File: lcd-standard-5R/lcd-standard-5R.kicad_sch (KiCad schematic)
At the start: 4 parts

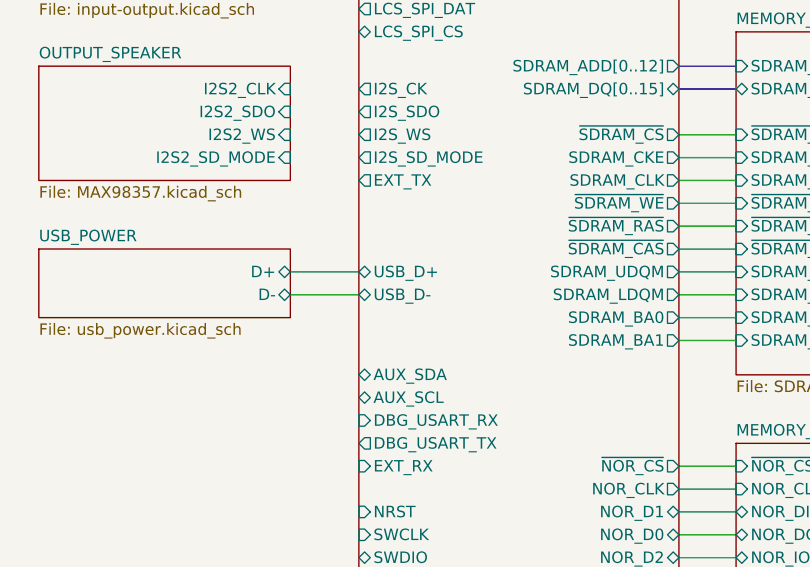
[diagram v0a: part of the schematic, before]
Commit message: Change pinout to the optimum usage
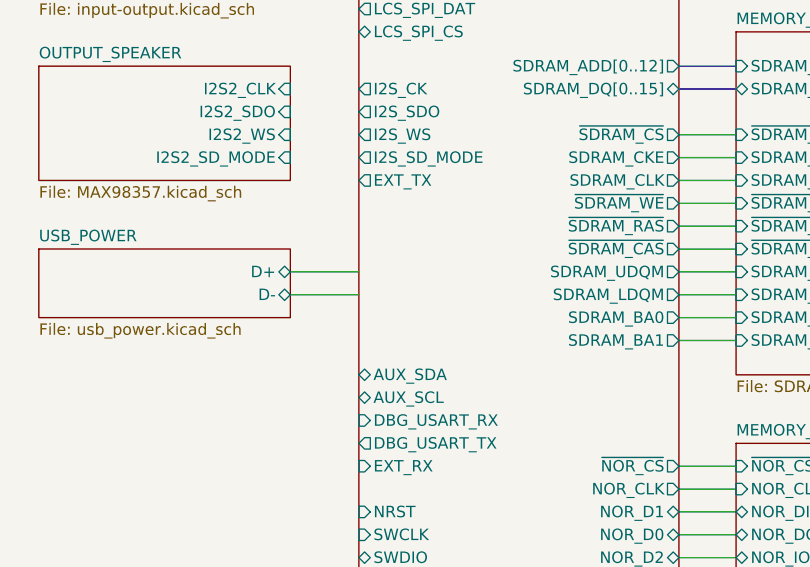
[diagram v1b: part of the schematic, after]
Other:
- sheet MCU ports: added none; removed USB_D+, USB_D-
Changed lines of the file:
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@@
-			)
-		)
-		(pin "USB_D-" bidirectional
-			(at 114.3 121.92 180)
-			(effects
-				(font
-					(size 1.27 1.27)
-				)
-				(justify left)
-			)
-		)
-		(pin "USB_D+" bidirectional
-			(at 114.3 119.38 180)
-			(effects
-				(font
-					(size 1.27 1.27)
-				)
-				(justify left)
 			)
 		)

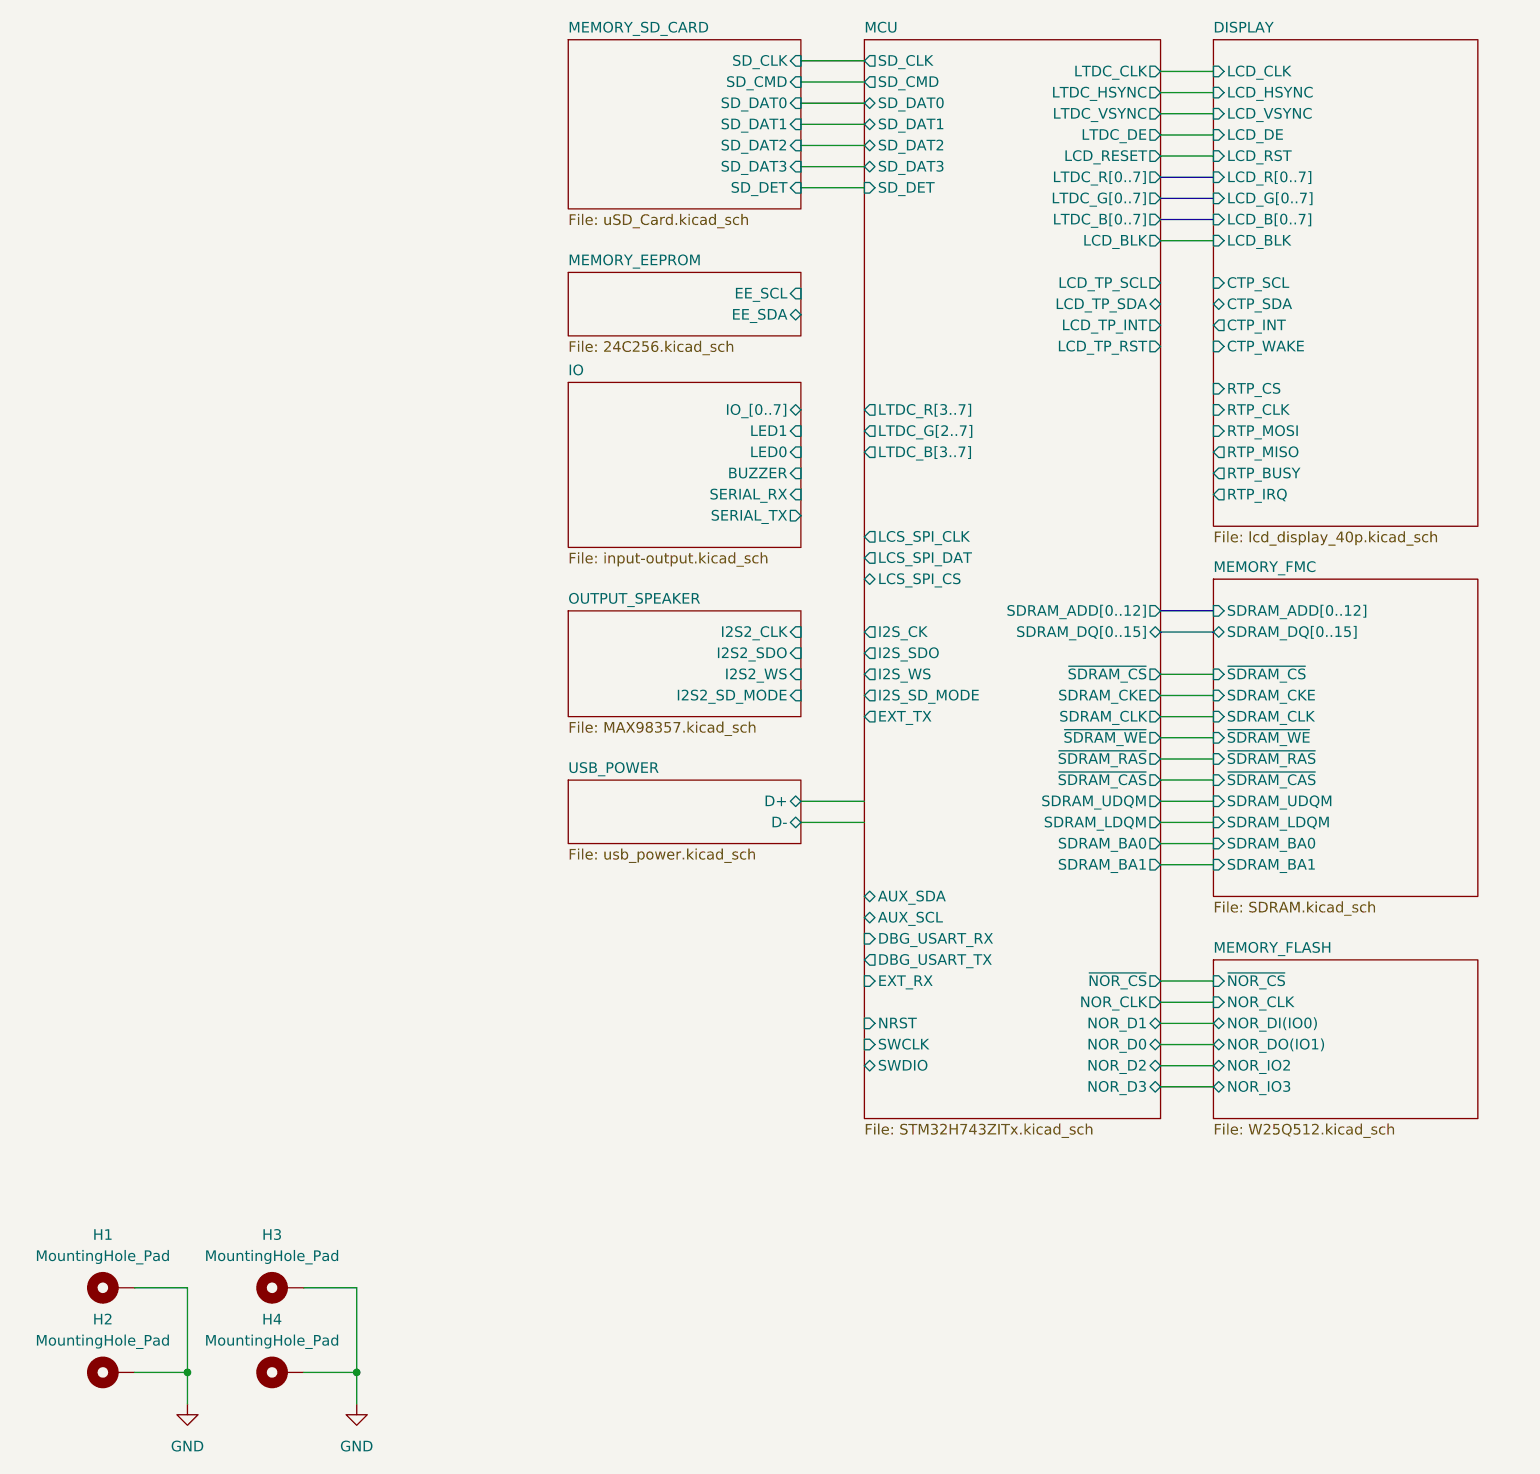
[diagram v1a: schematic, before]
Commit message: Finished SDRAM, LCD (need checkup with CubeIDE), RTP touch controll
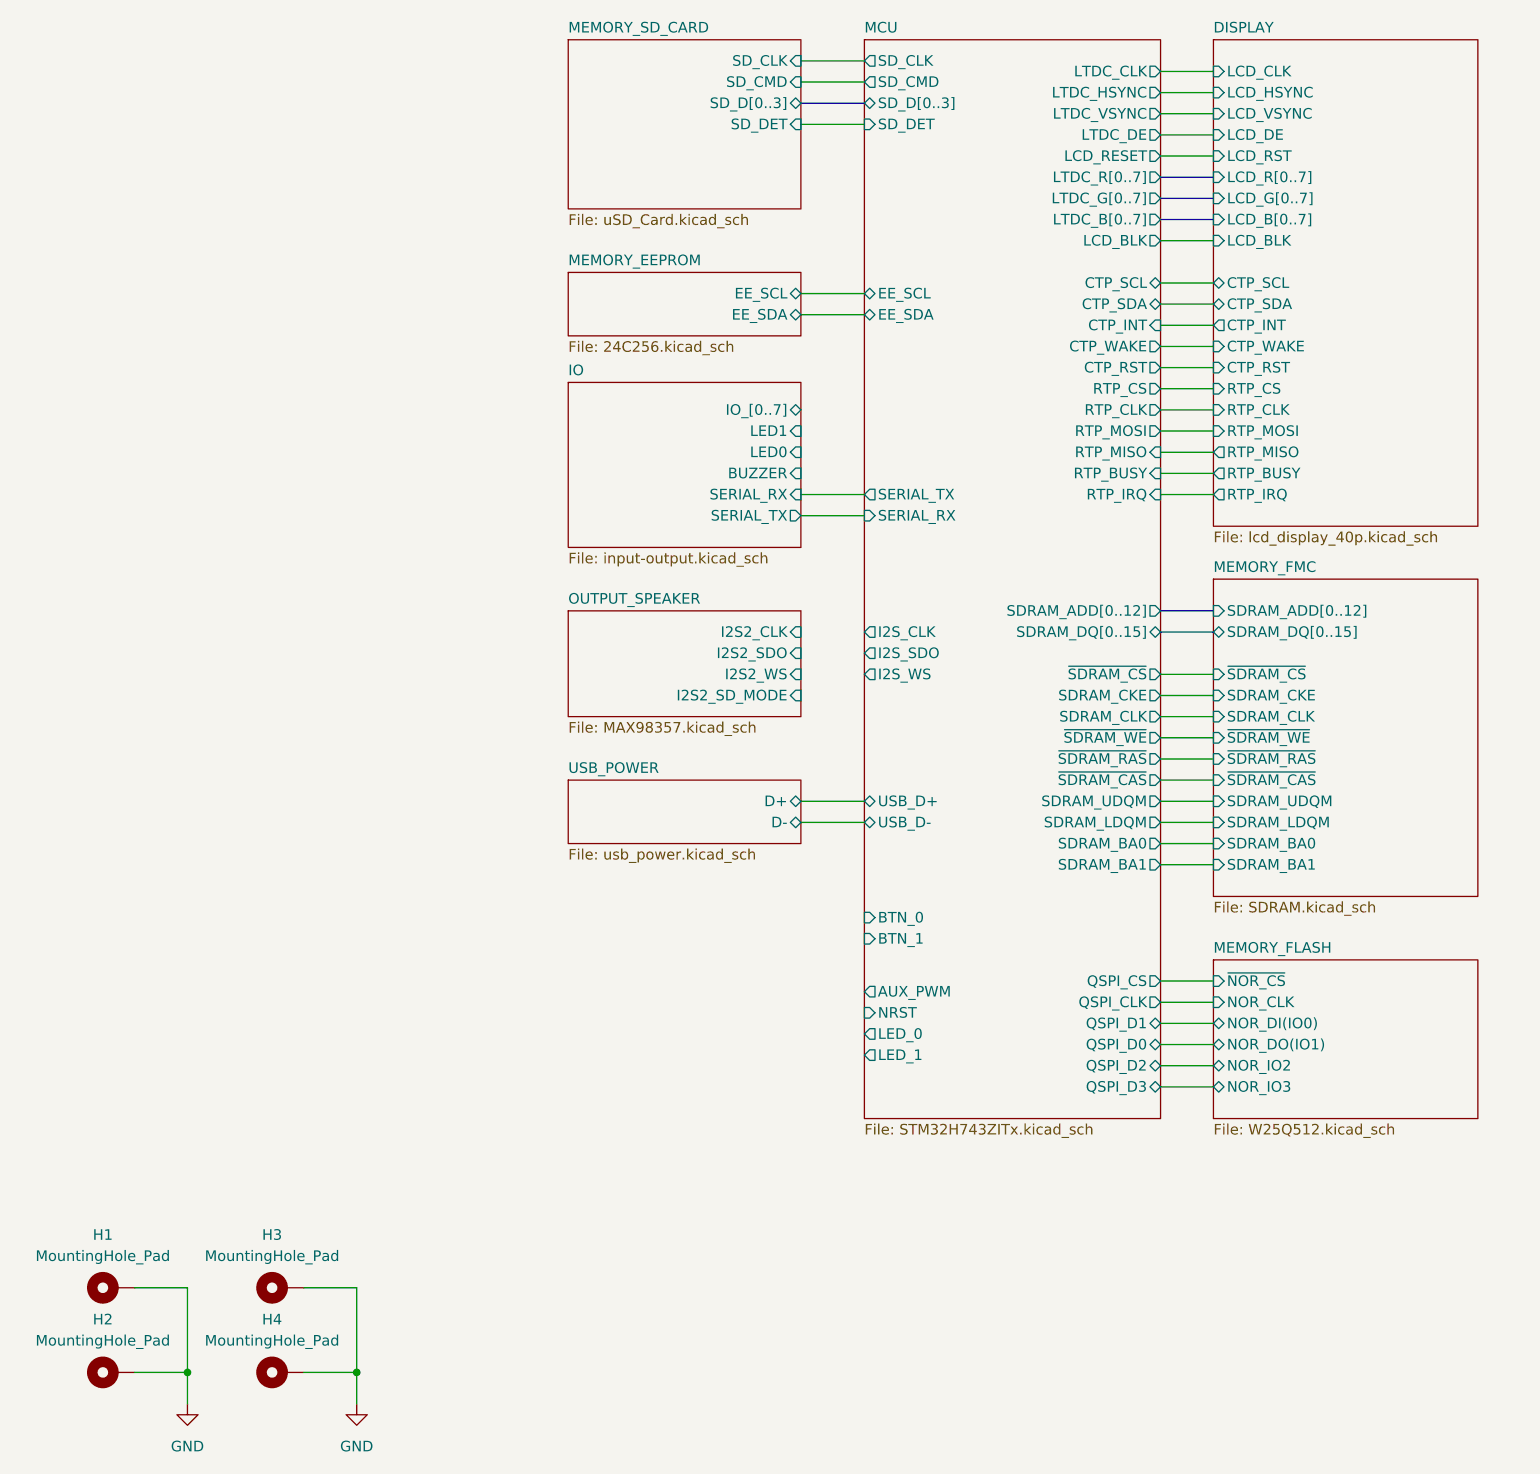
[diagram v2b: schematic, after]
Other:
- sheet DISPLAY ports: added CTP_RST; removed none
- sheet MCU ports: added AUX_PWM, BTN_0, BTN_1, CTP_INT, CTP_RST, CTP_SCL, CTP_SDA, CTP_WAKE, EE_SCL, EE_SDA, I2S_CLK, LED_0, LED_1, QSPI_CLK, QSPI_CS, QSPI_D0, QSPI_D1, QSPI_D2, QSPI_D3, RTP_BUSY, RTP_CLK, RTP_CS, RTP_IRQ, RTP_MISO, RTP_MOSI, SD_D[0..3], SERIAL_RX, SERIAL_TX, USB_D+, USB_D-; removed AUX_SCL, AUX_SDA, DBG_USART_RX, DBG_USART_TX, EXT_RX, EXT_TX, I2S_CK, I2S_SD_MODE, LCD_TP_INT, LCD_TP_RST, LCD_TP_SCL, LCD_TP_SDA, LCS_SPI_CLK, LCS_SPI_CS, LCS_SPI_DAT, LTDC_B[3..7], LTDC_G[2..7], LTDC_R[3..7], NOR_CLK, NOR_D0, NOR_D1, NOR_D2, NOR_D3, SD_DAT0, SD_DAT1, SD_DAT2, SD_DAT3, SWCLK, SWDIO, ~{NOR_CS}
- sheet MEMORY_SD_CARD ports: added SD_D[0..3]; removed SD_DAT0, SD_DAT1, SD_DAT2, SD_DAT3

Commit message: Finsihed, need to touch up a bit
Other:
- sheet IO ports: added BTN_0, BTN_1; removed none
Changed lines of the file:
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@@
+	(wire
+		(pts
+			(xy 106.68 80.01) (xy 114.3 80.01)
+		)
+		(stroke
+			(width 0)
+			(type default)
+		)
+	)
 	(wire
 		(pts
@@
 	(wire
 		(pts
+			(xy 106.68 124.46) (xy 114.3 124.46)
+		)
+		(stroke
+			(width 0)
+			(type default)
+		)
+	)
+	(wire
+		(pts
 			(xy 149.86 57.15) (xy 156.21 57.15)
 		)
@@
 	(wire
 		(pts
+			(xy 106.68 74.93) (xy 114.3 74.93)
+		)
+		(stroke
+			(width 0)
+			(type default)
+		)
+	)
+	(wire
+		(pts
 			(xy 149.86 143.51) (xy 156.21 143.51)
 		)
@@
 	(wire
 		(pts
-			(xy 106.68 85.09) (xy 114.3 85.09)
+			(xy 106.68 93.98) (xy 114.3 93.98)
 		)
 		(stroke
@@
 	(wire
 		(pts
+			(xy 106.68 127) (xy 114.3 127)
+		)
+		(stroke
+			(width 0)
+			(type default)
+		)
+	)
+	(wire
+		(pts
 			(xy 149.86 148.59) (xy 156.21 148.59)
 		)
@@
 	(wire
 		(pts
-			(xy 106.68 119.38) (xy 114.3 119.38)
+			(xy 106.68 142.24) (xy 114.3 142.24)
+		)
+		(stroke
+			(width 0)
+			(type default)
+		)
+	)
+	(wire
+		(pts
+			(xy 106.68 121.92) (xy 114.3 121.92)
 		)
 		(stroke
@@
 	(wire
 		(pts
+			(xy 106.68 77.47) (xy 114.3 77.47)
+		)
+		(stroke
+			(width 0)
+			(type default)
+		)
+	)
+	(wire
+		(pts
 			(xy 149.86 74.93) (xy 156.21 74.93)
 		)
@@
 	(wire
 		(pts
+			(xy 106.68 86.36) (xy 114.3 86.36)
+		)
+		(stroke
+			(width 0)
+			(type default)
+		)
+	)
+	(wire
+		(pts
 			(xy 149.86 121.92) (xy 156.21 121.92)
 		)
@@
 	(wire
 		(pts
-			(xy 106.68 121.92) (xy 114.3 121.92)
+			(xy 106.68 144.78) (xy 114.3 144.78)
 		)
 		(stroke
@@
 	(wire
 		(pts
+			(xy 106.68 82.55) (xy 114.3 82.55)
+		)
+		(stroke
+			(width 0)
+			(type default)
+		)
+	)
+	(wire
+		(pts
 			(xy 149.86 59.69) (xy 156.21 59.69)
 		)
@@
 	(wire
 		(pts
-			(xy 106.68 82.55) (xy 114.3 82.55)
+			(xy 106.68 91.44) (xy 114.3 91.44)
 		)
 		(stroke
@@
 	)
 	(sheet
-		(at 78.74 116.84)
+		(at 78.74 139.7)
 		(size 27.94 7.62)
 		(fields_autoplaced yes)
@@
 		)
 		(property "Sheetname" "USB_POWER"
-			(at 78.74 116.1284 0)
+			(at 78.74 138.9884 0)
 			(effects
 				(font
@@
 		)
 		(property "Sheetfile" "usb_power.kicad_sch"
-			(at 78.74 125.0446 0)
+			(at 78.74 147.9046 0)
 			(effects
 				(font
@@
 		)
 		(pin "D+" bidirectional
-			(at 106.68 119.38 0)
+			(at 106.68 142.24 0)
 			(effects
 				(font
@@
 		)
 		(pin "D-" bidirectional
-			(at 106.68 121.92 0)
+			(at 106.68 144.78 0)
 			(effects
 				(font
@@
 	)
 	(sheet
-		(at 78.74 96.52)
+		(at 78.74 119.38)
 		(size 27.94 12.7)
 		(fields_autoplaced yes)
@@
 		)
 		(property "Sheetname" "OUTPUT_SPEAKER"
-			(at 78.74 95.8084 0)
+			(at 78.74 118.6684 0)
 			(effects
 				(font
@@
 		)
 		(property "Sheetfile" "MAX98357.kicad_sch"
-			(at 78.74 109.8046 0)
+			(at 78.74 132.6646 0)
 			(effects
 				(font
@@
 		)
 		(pin "I2S2_CLK" input
-			(at 106.68 99.06 0)
+			(at 106.68 121.92 0)
 			(effects
 				(font
@@
 		)
 		(pin "I2S2_SDO" input
-			(at 106.68 101.6 0)
+			(at 106.68 124.46 0)
 			(effects
 				(font
@@
 		)
 		(pin "I2S2_WS" input
-			(at 106.68 104.14 0)
+			(at 106.68 127 0)
 			(effects
 				(font
@@
 		)
 		(pin "I2S2_SD_MODE" input
-			(at 106.68 106.68 0)
+			(at 106.68 129.54 0)
 			(effects
 				(font
@@
 		)
 		(pin "SERIAL_TX" output
-			(at 114.3 82.55 180)
+			(at 114.3 91.44 180)
 			(effects
 				(font
@@
 		)
 		(pin "SERIAL_RX" input
-			(at 114.3 85.09 180)
+			(at 114.3 93.98 180)
 			(effects
 				(font
@@
 		)
 		(pin "USB_D-" bidirectional
-			(at 114.3 121.92 180)
+			(at 114.3 144.78 180)
 			(effects
 				(font
@@
 		)
 		(pin "USB_D+" bidirectional
-			(at 114.3 119.38 180)
+			(at 114.3 142.24 180)
 			(effects
 				(font
@@
 		)
 		(pin "NRST" input
-			(at 114.3 144.78 180)
+			(at 114.3 154.94 180)
 			(effects
 				(font
@@
 		)
 		(pin "AUX_PWM" output
-			(at 114.3 142.24 180)
+			(at 114.3 86.36 180)
 			(effects
 				(font
@@
 		)
 		(pin "I2S_WS" output
-			(at 114.3 104.14 180)
+			(at 114.3 127 180)
 			(effects
 				(font
@@
 		)
 		(pin "LED_0" output
-			(at 114.3 147.32 180)
+			(at 114.3 77.47 180)
 			(effects
 				(font
@@
 		)
 		(pin "LED_1" output
-			(at 114.3 149.86 180)
+			(at 114.3 74.93 180)
 			(effects
 				(font
@@
 		)
 		(pin "BTN_1" input
-			(at 114.3 135.89 180)
+			(at 114.3 82.55 180)
 			(effects
 				(font
@@
 		)
 		(pin "BTN_0" input
-			(at 114.3 133.35 180)
+			(at 114.3 80.01 180)
 			(effects
 				(font
@@
 		)
 		(pin "I2S_CLK" output
-			(at 114.3 99.06 180)
+			(at 114.3 121.92 180)
 			(effects
 				(font
@@
 		)
 		(pin "I2S_SDO" output
-			(at 114.3 101.6 180)
+			(at 114.3 124.46 180)
 			(effects
 				(font
@@
 	(sheet
 		(at 78.74 69.088)
-		(size 27.94 19.812)
+		(size 27.94 28.702)
 		(fields_autoplaced yes)
 		(stroke
@@
 		)
 		(property "Sheetfile" "input-output.kicad_sch"
-			(at 78.74 89.4846 0)
+			(at 78.74 98.3746 0)
 			(effects
 				(font
@@
 		)
 		(pin "BUZZER" input
+			(at 106.68 86.36 0)
+			(effects
+				(font
+					(size 1.27 1.27)
+				)
+				(justify right)
+			)
+		)
+		(pin "SERIAL_RX" input
+			(at 106.68 91.44 0)
+			(effects
+				(font
+					(size 1.27 1.27)
+				)
+				(justify right)
+			)
+		)
+		(pin "SERIAL_TX" output
+			(at 106.68 93.98 0)
+			(effects
+				(font
+					(size 1.27 1.27)
+				)
+				(justify right)
+			)
+		)
+		(pin "BTN_0" output
 			(at 106.68 80.01 0)
 			(effects
@@
 			)
 		)
-		(pin "SERIAL_RX" input
+		(pin "BTN_1" output
 			(at 106.68 82.55 0)
 			(effects
 				(font
-					(size 1.27 1.27)
-				)
-				(justify right)
-			)
-		)
-		(pin "SERIAL_TX" output
-			(at 106.68 85.09 0)
-			(effects
-				(font

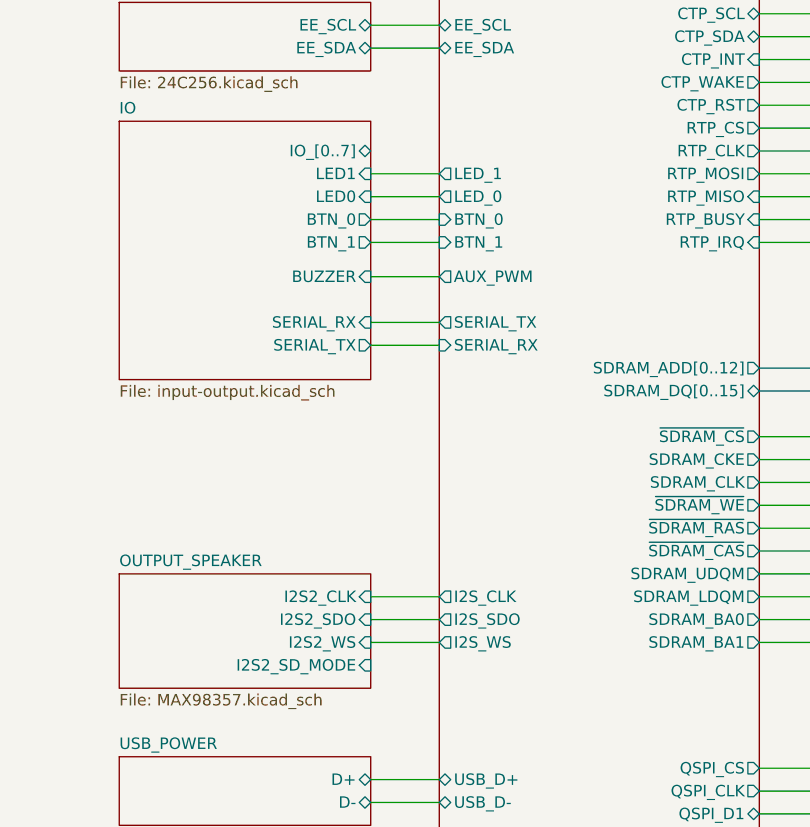
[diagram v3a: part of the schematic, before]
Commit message: Adding filter on MAX98357, TODO: Add more grounding vias
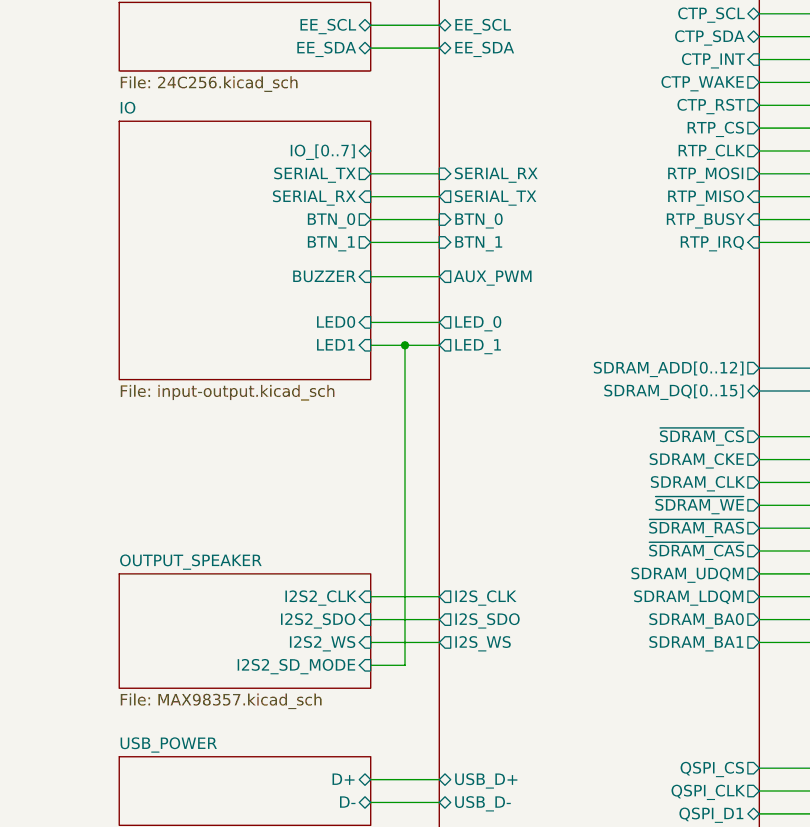
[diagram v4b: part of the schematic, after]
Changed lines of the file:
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@@
 		(color 0 0 0 0)
 	)
+	(junction
+		(at 110.49 93.98)
+		(diameter 0)
+		(color 0 0 0 0)
+	)
 	(wire
 		(pts
@@
 	(wire
 		(pts
+			(xy 106.68 129.54) (xy 110.49 129.54)
+		)
+		(stroke
+			(width 0)
+			(type default)
+		)
+	)
+	(wire
+		(pts
 			(xy 149.86 140.97) (xy 156.21 140.97)
 		)
@@
 	(wire
 		(pts
+			(xy 110.49 93.98) (xy 110.49 129.54)
+		)
+		(stroke
+			(width 0)
+			(type default)
+		)
+	)
+	(wire
+		(pts
+			(xy 110.49 93.98) (xy 114.3 93.98)
+		)
+		(stroke
+			(width 0)
+			(type default)
+		)
+	)
+	(wire
+		(pts
 			(xy 106.68 58.42) (xy 114.3 58.42)
 		)
@@
 	(wire
 		(pts
-			(xy 106.68 93.98) (xy 114.3 93.98)
+			(xy 106.68 93.98) (xy 110.49 93.98)
 		)
 		(stroke
@@
 		)
 		(pin "SERIAL_TX" output
-			(at 114.3 91.44 180)
+			(at 114.3 77.47 180)
 			(effects
 				(font
@@
 		)
 		(pin "SERIAL_RX" input
-			(at 114.3 93.98 180)
+			(at 114.3 74.93 180)
 			(effects
 				(font
@@
 		)
 		(pin "LED_0" output
-			(at 114.3 77.47 180)
+			(at 114.3 91.44 180)
 			(effects
 				(font
@@
 		)
 		(pin "LED_1" output
-			(at 114.3 74.93 180)
+			(at 114.3 93.98 180)
 			(effects
 				(font
@@
 		)
 		(pin "LED1" input
-			(at 106.68 74.93 0)
+			(at 106.68 93.98 0)
 			(effects
 				(font
@@
 		)
 		(pin "LED0" input
-			(at 106.68 77.47 0)
+			(at 106.68 91.44 0)
 			(effects
 				(font
@@
 		)
 		(pin "SERIAL_RX" input
-			(at 106.68 91.44 0)
+			(at 106.68 77.47 0)
 			(effects
 				(font
@@
 		)
 		(pin "SERIAL_TX" output
-			(at 106.68 93.98 0)
-			(effects
-				(font
+			(at 106.68 74.93 0)
+			(effects
+				(font
